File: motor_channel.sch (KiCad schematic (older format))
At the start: 1 part

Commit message: added jtag programming header for uC
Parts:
- U?: symbol hbridge:PWD13F60 -> bangbang_rev1-rescue:PWD13F60-hbridge
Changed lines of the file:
@@
 EESchema Schematic File Version 4
-LIBS:bangbang_rev1-cache
 EELAYER 30 0
 EELAYER END
@@
 $EndDescr
 $Comp
-L hbridge:PWD13F60 U?
+L bangbang_rev1-rescue:PWD13F60-hbridge U?
 U 1 1 5E507B4D
 P 3450 2900
+AR Path="/5E507B4D" Ref="U?"  Part="1"
+AR Path="/5E49EA18/5E507A5C/5E507B4D" Ref="U?"  Part="1"
 F 0 "U?" H 3450 3667 50  0000 C CNN
 F 1 "PWD13F60" H 3450 3576 50  0000 C CNN

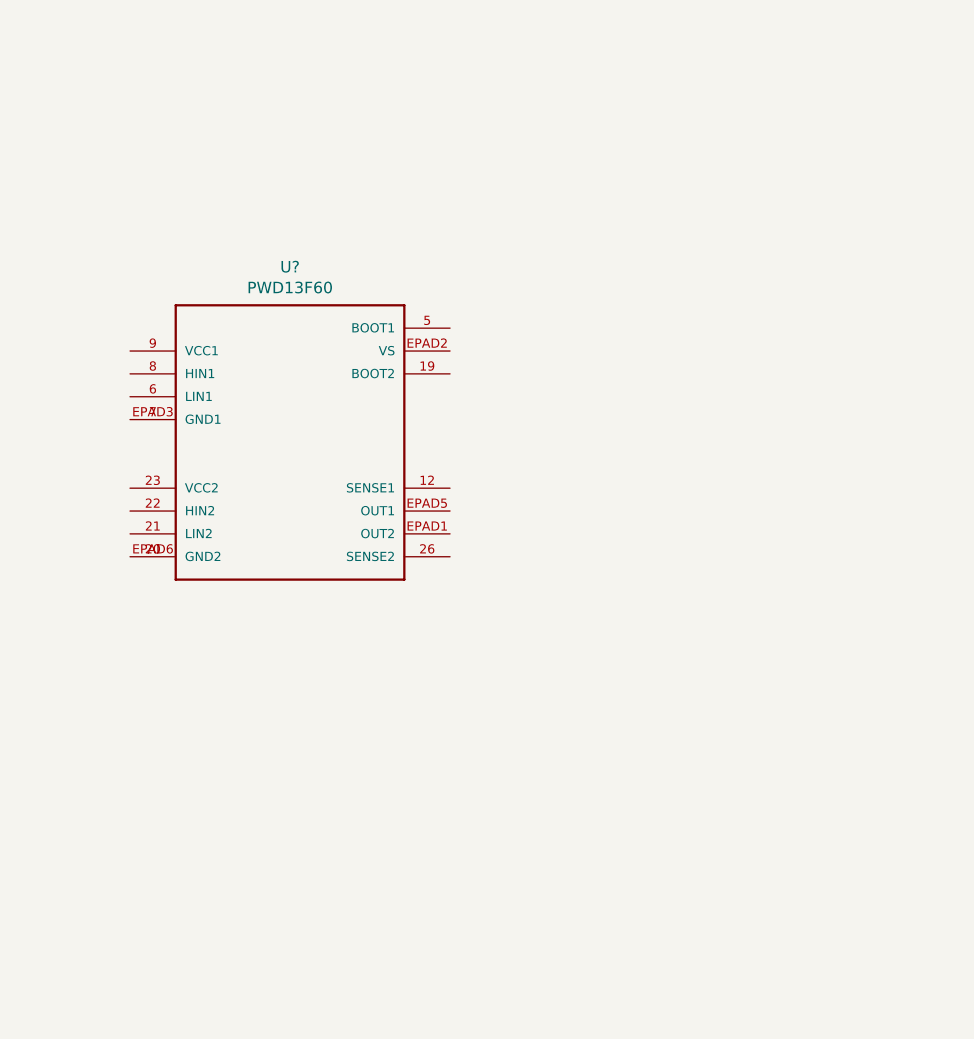
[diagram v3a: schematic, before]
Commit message: Motor channels mostly finished
Todo: Need to determine capacitance of decoupling caps in motor channel.
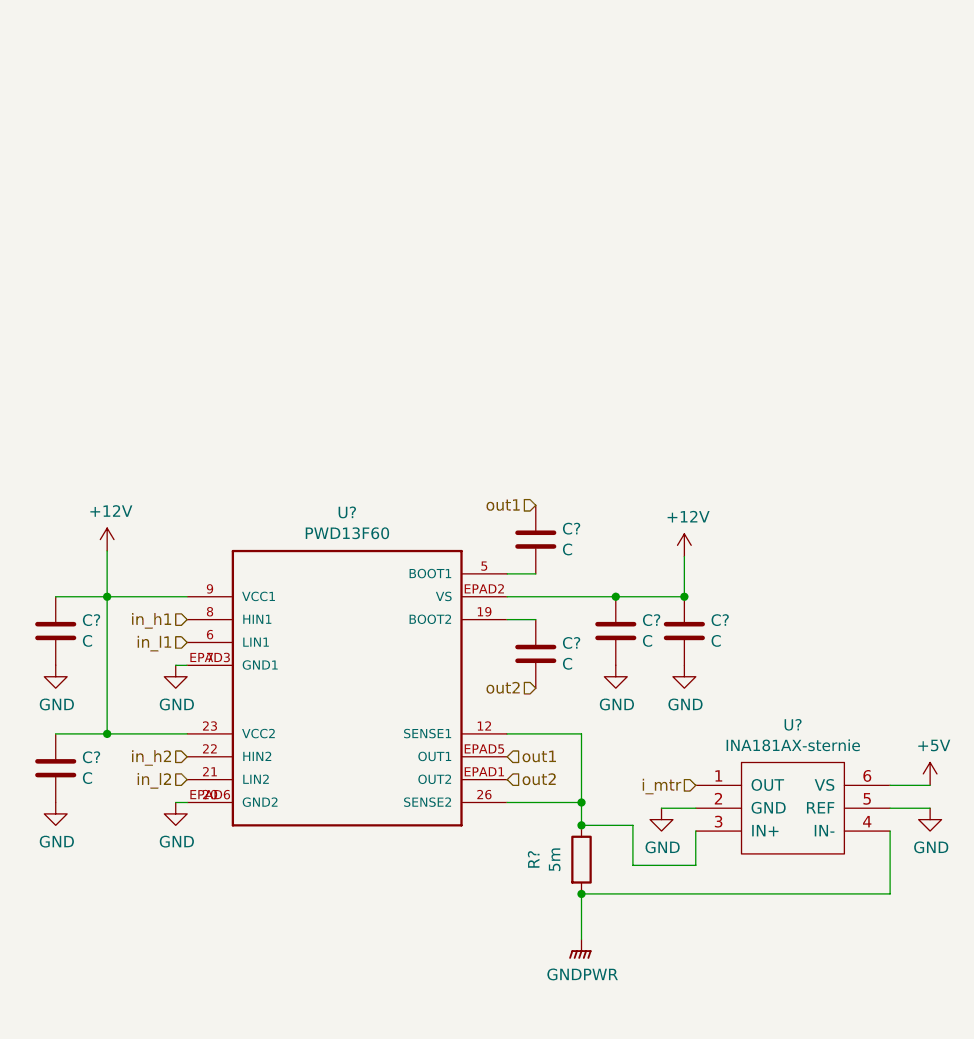
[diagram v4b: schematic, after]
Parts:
- added C? (x6): C, symbol Device:C
- added R?: 5m, symbol Device:R
- added U?: INA181AX-sternie, symbol bangbang_rev1-rescue:INA181AX-sternie
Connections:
- net at U?.12 (SENSE1): now also U?.26 (SENSE2), R?.1, U?.3 (IN+)
- net at U?.19 (BOOT2): now also C?.1
- net GND: now reaches U?.20 (GND2), U?.EPAD6 (GND2)
- net GND: now also U?.7 (GND1), U?.EPAD3 (GND1), C?.2, C?.2, C?.2, C?.2, U?.2 (GND), U?.5 (REF)
- net in_l2: now reaches U?.21 (LIN2)
- net in_h2: now reaches U?.22 (HIN2)
- net +12V: now reaches U?.23 (VCC2)
- net +12V: now also U?.9 (VCC1), U?.EPAD2 (VS), C?.1, C?.1, C?.1, C?.1
- net at U?.5 (BOOT1): now also C?.2
- net in_l1: now reaches U?.6 (LIN1)
- net in_h1: now reaches U?.8 (HIN1)
- net out2: now reaches U?.EPAD1 (OUT2)
- net out2: now also C?.2
- net out1: now reaches U?.EPAD5 (OUT1)
- net out1: now also C?.1
- new net +5V: U?.6 (VS)
- new net GNDPWR: R?.2, U?.4 (IN-)
- new net i_mtr: U?.1 (OUT)
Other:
- moved on the sheet: U?

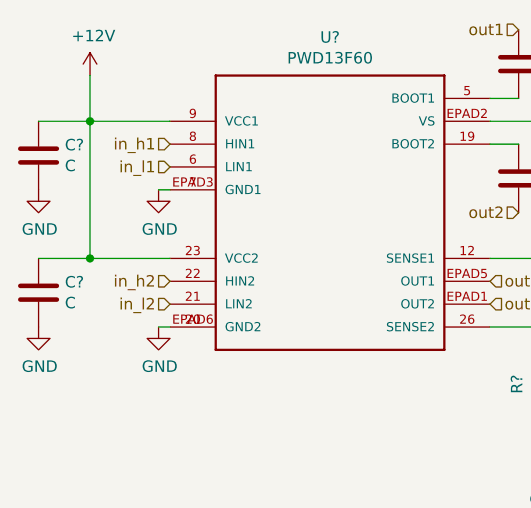
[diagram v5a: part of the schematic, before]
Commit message: Updated Motor Channels
Each motor only needs two inputs.
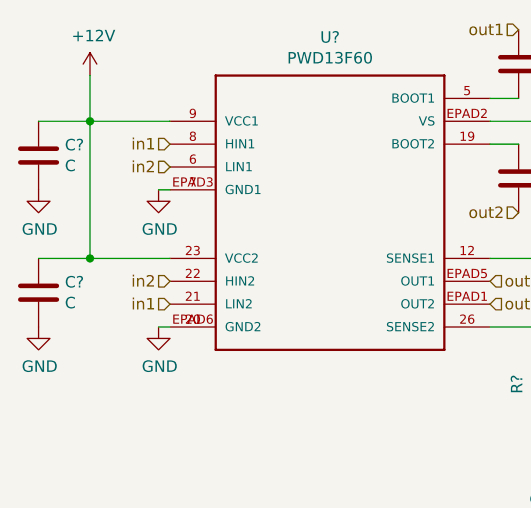
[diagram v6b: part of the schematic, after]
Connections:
- net in_l1 is gone; now on net in2: U?.6 (LIN1)
- net in_l2 is gone; now on net in1: U?.21 (LIN2)
- net in_h1 renamed in1
- net in_h2 renamed in2
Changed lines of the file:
@@
 AR Path="/5E49EA18/5E507A5C/5E507B4D" Ref="U?"  Part="1"
 AR Path="/5E49EA18/5E6AD26A/5E507B4D" Ref="U?"  Part="1"
+AR Path="/5E49EA18/5E6EF1BC/5E507B4D" Ref="U?"  Part="1"
 F 0 "U?" H 3700 4742 50  0000 C CNN
 F 1 "PWD13F60" H 3700 4651 50  0000 C CNN
@@
 AR Path="/5E49EA18/5E507A5C/5E6371F6" Ref="R?"  Part="1"
 AR Path="/5E49EA18/5E6AD26A/5E6371F6" Ref="R?"  Part="1"
+AR Path="/5E49EA18/5E6EF1BC/5E6371F6" Ref="R?"  Part="1"
 F 0 "R?" V 4518 4725 50  0000 C CNN
 F 1 "5m" V 4609 4725 50  0000 C CNN
@@
 AR Path="/5E49EA18/5E507A5C/5E634929" Ref="U?"  Part="1"
 AR Path="/5E49EA18/5E6AD26A/5E634929" Ref="U?"  Part="1"
+AR Path="/5E49EA18/5E6EF1BC/5E634929" Ref="U?"  Part="1"
 F 0 "U?" H 5650 4863 49  0000 C CNN
 F 1 "INA181AX-sternie" H 5650 4773 49  0000 C CNN
@@
 AR Path="/5E49EA18/5E507A5C/5E660BF5" Ref="#PWR?"  Part="1"
 AR Path="/5E49EA18/5E6AD26A/5E660BF5" Ref="#PWR?"  Part="1"
+AR Path="/5E49EA18/5E6EF1BC/5E660BF5" Ref="#PWR?"  Part="1"
 F 0 "#PWR?" H 6250 4250 50  0001 C CNN
 F 1 "GND" H 6255 4327 50  0000 C CNN
@@
 AR Path="/5E49EA18/5E507A5C/5E66287A" Ref="#PWR?"  Part="1"
 AR Path="/5E49EA18/5E6AD26A/5E66287A" Ref="#PWR?"  Part="1"
+AR Path="/5E49EA18/5E6EF1BC/5E66287A" Ref="#PWR?"  Part="1"
 F 0 "#PWR?" H 6250 4250 50  0001 C CNN
 F 1 "+5V" H 6265 4573 50  0000 C CNN
@@
 AR Path="/5E49EA18/5E507A5C/5E663717" Ref="#PWR?"  Part="1"
 AR Path="/5E49EA18/5E6AD26A/5E663717" Ref="#PWR?"  Part="1"
+AR Path="/5E49EA18/5E6EF1BC/5E663717" Ref="#PWR?"  Part="1"
 F 0 "#PWR?" H 5075 4250 50  0001 C CNN
 F 1 "GND" H 5080 4327 50  0000 C CNN
@@
 AR Path="/5E49EA18/5E507A5C/5E685700" Ref="#PWR?"  Part="1"
 AR Path="/5E49EA18/5E6AD26A/5E685700" Ref="#PWR?"  Part="1"
+AR Path="/5E49EA18/5E6EF1BC/5E685700" Ref="#PWR?"  Part="1"
 F 0 "#PWR?" H 2650 3225 50  0001 C CNN
 F 1 "+12V" H 2665 3548 50  0000 C CNN
@@
 	4725 4475 4400 4475
 Text HLabel 3000 3675 0    50   Input ~ 0
-in_h1
+in1
 Text HLabel 3000 3775 0    50   Input ~ 0
-in_l1
+in2
 Text HLabel 3000 4275 0    50   Input ~ 0
-in_h2
+in2
 Text HLabel 3000 4375 0    50   Input ~ 0
-in_l2
+in1
 Wire Wire Line
 	2650 4175 2650 3575
@@
 U 1 1 5E6C0524
 P 4725 5075
+AR Path="/5E49EA18/5E507A5C/5E6C0524" Ref="#PWR?"  Part="1"
+AR Path="/5E49EA18/5E6EF1BC/5E6C0524" Ref="#PWR?"  Part="1"
 F 0 "#PWR?" H 4725 4875 50  0001 C CNN
 F 1 "GNDPWR" H 4729 4921 50  0000 C CNN
@@
 U 1 1 5E6C2BF6
 P 2950 3875
+AR Path="/5E49EA18/5E507A5C/5E6C2BF6" Ref="#PWR?"  Part="1"
+AR Path="/5E49EA18/5E6EF1BC/5E6C2BF6" Ref="#PWR?"  Part="1"
 F 0 "#PWR?" H 2950 3625 50  0001 C CNN
 F 1 "GND" H 2955 3702 50  0000 C CNN
@@
 U 1 1 5E6C314D
 P 2950 4475
+AR Path="/5E49EA18/5E507A5C/5E6C314D" Ref="#PWR?"  Part="1"
+AR Path="/5E49EA18/5E6EF1BC/5E6C314D" Ref="#PWR?"  Part="1"
 F 0 "#PWR?" H 2950 4225 50  0001 C CNN
 F 1 "GND" H 2955 4302 50  0000 C CNN
@@
 U 1 1 5E6C3B2F
 P 2425 3725
+AR Path="/5E49EA18/5E507A5C/5E6C3B2F" Ref="C?"  Part="1"
+AR Path="/5E49EA18/5E6EF1BC/5E6C3B2F" Ref="C?"  Part="1"
 F 0 "C?" H 2540 3771 50  0000 L CNN
 F 1 "C" H 2540 3680 50  0000 L CNN
@@
 U 1 1 5E6C48A1
 P 2425 4325
+AR Path="/5E49EA18/5E507A5C/5E6C48A1" Ref="C?"  Part="1"
+AR Path="/5E49EA18/5E6EF1BC/5E6C48A1" Ref="C?"  Part="1"
 F 0 "C?" H 2540 4371 50  0000 L CNN
 F 1 "C" H 2540 4280 50  0000 L CNN
@@
 U 1 1 5E6C5CF4
 P 2425 3875
+AR Path="/5E49EA18/5E507A5C/5E6C5CF4" Ref="#PWR?"  Part="1"
+AR Path="/5E49EA18/5E6EF1BC/5E6C5CF4" Ref="#PWR?"  Part="1"
 F 0 "#PWR?" H 2425 3625 50  0001 C CNN
 F 1 "GND" H 2430 3702 50  0000 C CNN
@@
 U 1 1 5E6C6240
 P 2425 4475
+AR Path="/5E49EA18/5E507A5C/5E6C6240" Ref="#PWR?"  Part="1"
+AR Path="/5E49EA18/5E6EF1BC/5E6C6240" Ref="#PWR?"  Part="1"
 F 0 "#PWR?" H 2425 4225 50  0001 C CNN
 F 1 "GND" H 2430 4302 50  0000 C CNN
@@
 U 1 1 5E6C6CA0
 P 4525 3325
+AR Path="/5E49EA18/5E507A5C/5E6C6CA0" Ref="C?"  Part="1"
+AR Path="/5E49EA18/5E6EF1BC/5E6C6CA0" Ref="C?"  Part="1"
 F 0 "C?" H 4640 3371 50  0000 L CNN
 F 1 "C" H 4640 3280 50  0000 L CNN
@@
 U 1 1 5E6C896D
 P 4525 3825
+AR Path="/5E49EA18/5E507A5C/5E6C896D" Ref="C?"  Part="1"
+AR Path="/5E49EA18/5E6EF1BC/5E6C896D" Ref="C?"  Part="1"
 F 0 "C?" H 4640 3871 50  0000 L CNN
 F 1 "C" H 4640 3780 50  0000 L CNN
@@
 U 1 1 5E6CC77E
 P 5175 3400
+AR Path="/5E49EA18/5E507A5C/5E6CC77E" Ref="#PWR?"  Part="1"
+AR Path="/5E49EA18/5E6EF1BC/5E6CC77E" Ref="#PWR?"  Part="1"
 F 0 "#PWR?" H 5175 3250 50  0001 C CNN
 F 1 "+12V" H 5190 3573 50  0000 C CNN
@@
 U 1 1 5E6CD1E7
 P 4875 3725
+AR Path="/5E49EA18/5E507A5C/5E6CD1E7" Ref="C?"  Part="1"
+AR Path="/5E49EA18/5E6EF1BC/5E6CD1E7" Ref="C?"  Part="1"
 F 0 "C?" H 4990 3771 50  0000 L CNN
 F 1 "C" H 4990 3680 50  0000 L CNN
@@
 U 1 1 5E6CE986
 P 5175 3725
+AR Path="/5E49EA18/5E507A5C/5E6CE986" Ref="C?"  Part="1"
+AR Path="/5E49EA18/5E6EF1BC/5E6CE986" Ref="C?"  Part="1"
 F 0 "C?" H 5290 3771 50  0000 L CNN
 F 1 "C" H 5290 3680 50  0000 L CNN
@@
 U 1 1 5E6D07E0
 P 4875 3875
+AR Path="/5E49EA18/5E507A5C/5E6D07E0" Ref="#PWR?"  Part="1"
+AR Path="/5E49EA18/5E6EF1BC/5E6D07E0" Ref="#PWR?"  Part="1"
 F 0 "#PWR?" H 4875 3625 50  0001 C CNN
 F 1 "GND" H 4880 3702 50  0000 C CNN
@@
 U 1 1 5E6D0C7C
 P 5175 3875
+AR Path="/5E49EA18/5E507A5C/5E6D0C7C" Ref="#PWR?"  Part="1"
+AR Path="/5E49EA18/5E6EF1BC/5E6D0C7C" Ref="#PWR?"  Part="1"
 F 0 "#PWR?" H 5175 3625 50  0001 C CNN
 F 1 "GND" H 5180 3702 50  0000 C CNN

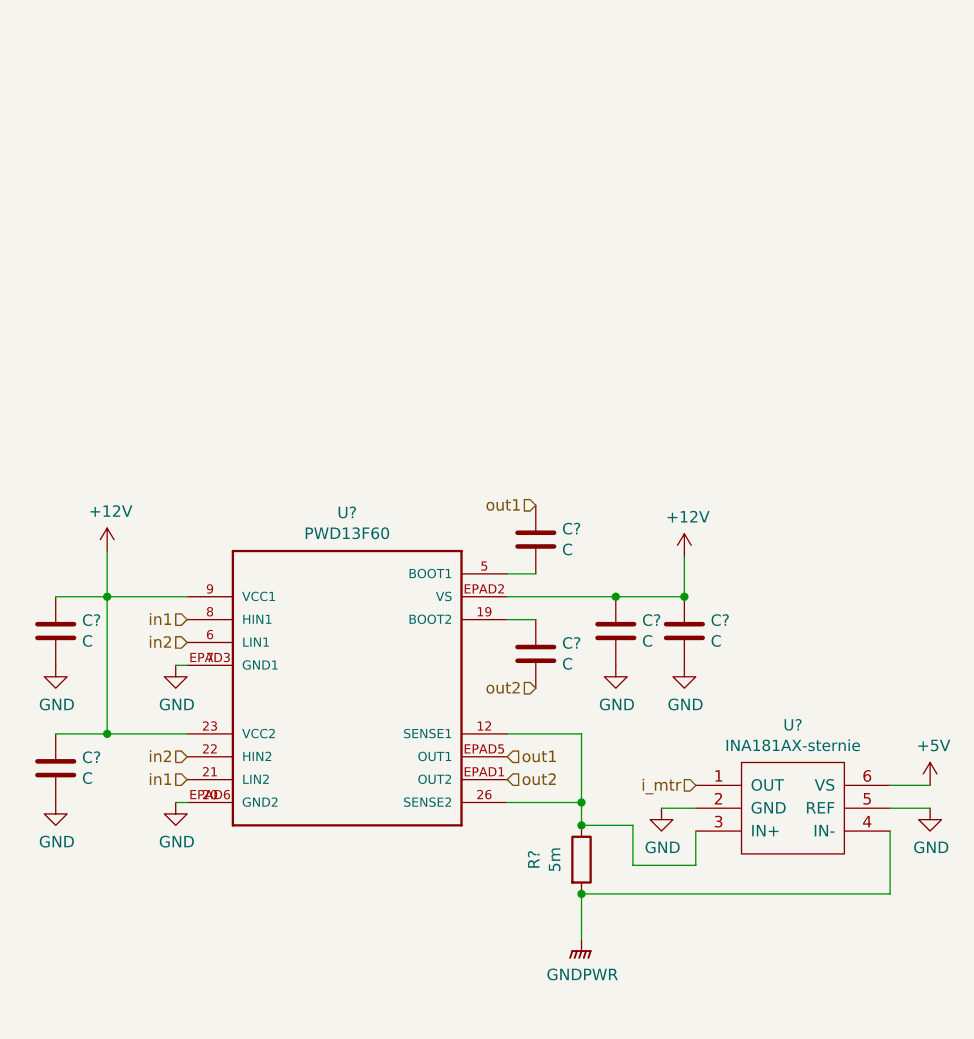
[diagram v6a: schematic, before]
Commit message: added dual inpt and gate control
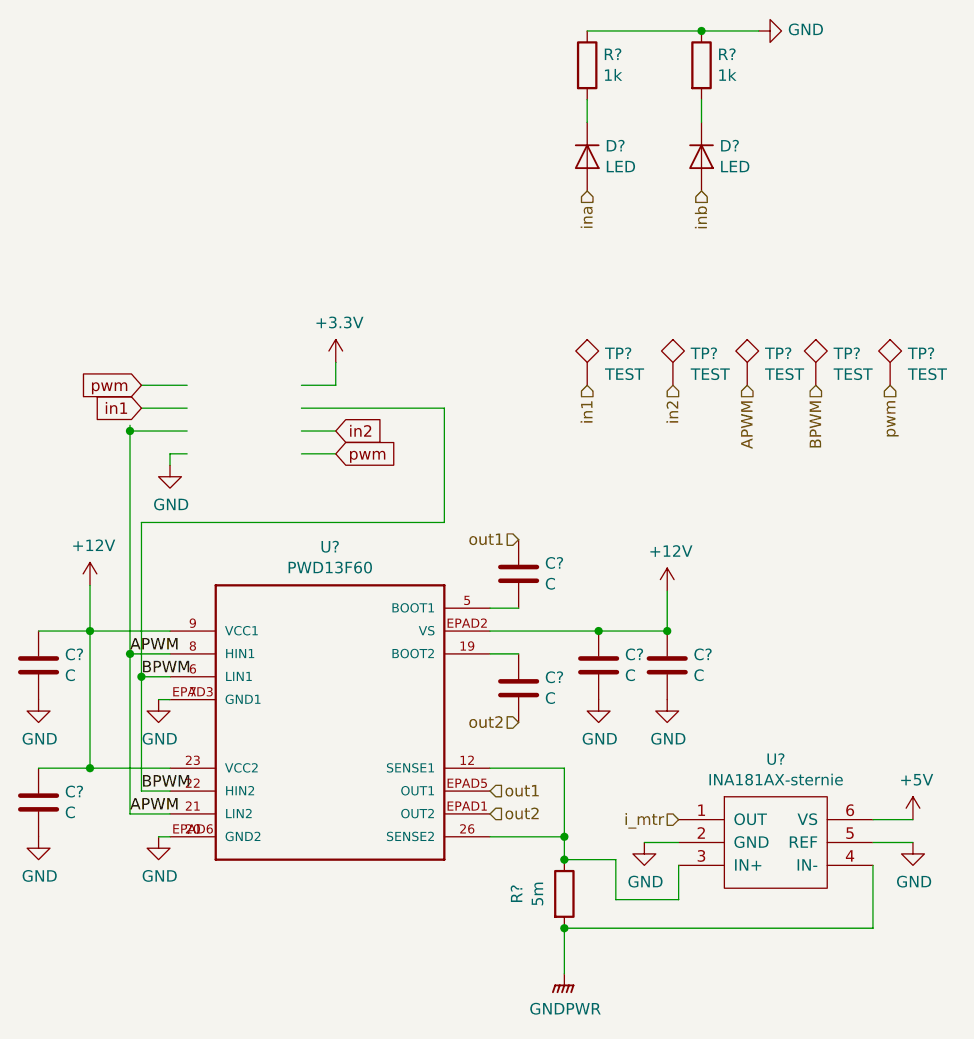
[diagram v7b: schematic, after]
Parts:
- added D? (x2): LED, symbol Device:D
- added R? (x2): 1k, symbol Device:R
- added TP? (x5): TEST, symbol Engine_Controller-cache:TEST
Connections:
- net labels added: +3.3V, APWM, BPWM, ina, inb, pwm
- wire segments 27 -> 52
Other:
- moved on the sheet: C?, R?, U?

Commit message: Added AND gate footprint
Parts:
- added U?: 74AHC2G08, symbol ec_2b_rescue:74AHC2G08
- TP? (x5): symbol Engine_Controller-cache:TEST -> bangbang_rev1-rescue:TEST-Engine_Controller-cache
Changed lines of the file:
@@
 $Descr A4 11693 8268
 encoding utf-8
-Sheet 12 12
+Sheet 11 12
 Title ""
 Date ""
@@
 in1
 Wire Wire Line
-	3500 2650 3650 2650
-Wire Wire Line
-	3650 2650 3650 2550
-Wire Wire Line
-	3500 2850 3650 2850
-Wire Wire Line
-	3500 2950 3650 2950
-Text GLabel 3650 2850 2    50   Input ~ 0
+	3900 2650 4050 2650
+Wire Wire Line
+	4050 2650 4050 2550
+Wire Wire Line
+	3900 2850 4050 2850
+Wire Wire Line
+	3900 2950 4050 2950
+Text GLabel 4050 2850 2    50   Input ~ 0
 in2
-Text GLabel 3650 2950 2    50   Input ~ 0
+Text GLabel 4050 2950 2    50   Input ~ 0
 pwm
 Wire Wire Line
@@
 	2750 3825 2750 4525
 Wire Wire Line
-	4125 2750 4125 3250
-Wire Wire Line
-	4125 3250 2800 3250
-Wire Wire Line
 	2800 3250 2800 3925
 Wire Wire Line
 	2800 4425 2925 4425
-Wire Wire Line
-	3500 2750 4125 2750
 Wire Wire Line
 	2925 3925 2800 3925
@@
 L power:+3.3V #PWR?
 U 1 1 5E666730
-P 3650 2550
+P 4050 2550
 AR Path="/5E49EA18/5E507A5C/5E666730" Ref="#PWR?"  Part="1"
 AR Path="/5E49EA18/5E6EF1BC/5E666730" Ref="#PWR?"  Part="1"
-F 0 "#PWR?" H 3650 2400 50  0001 C CNN
-F 1 "+3.3V" H 3665 2723 50  0000 C CNN
-F 2 "" H 3650 2550 50  0001 C CNN
-F 3 "" H 3650 2550 50  0001 C CNN
-	1    3650 2550
+F 0 "#PWR?" H 4050 2400 50  0001 C CNN
+F 1 "+3.3V" H 4065 2723 50  0000 C CNN
+F 2 "" H 4050 2550 50  0001 C CNN
+F 3 "" H 4050 2550 50  0001 C CNN
+	1    4050 2550
 	1    0    0    -1
 $EndComp
@@
 	2925 2950 3000 2950
 $Comp
-L Engine_Controller-cache:GND #PWR?
+L bangbang_rev1-rescue:GND-Engine_Controller-cache #PWR?
 U 1 1 5E669D2E
 P 2925 3000
 AR Path="/5E49EA18/5E507A5C/5E669D2E" Ref="#PWR?"  Part="1"
 AR Path="/5E49EA18/5E6EF1BC/5E669D2E" Ref="#PWR?"  Part="1"
+AR Path="/5E669D2E" Ref="#PWR?"  Part="1"
 F 0 "#PWR?" H 2925 2750 50  0001 C CNN
 F 1 "GND" H 2930 2827 50  0000 C CNN
@@
 $EndComp
 $Comp
-L Engine_Controller-cache:TEST TP?
+L bangbang_rev1-rescue:TEST-Engine_Controller-cache TP?
 U 1 1 5E66AC4A
 P 4750 2650
@@
 $EndComp
 $Comp
-L Engine_Controller-cache:TEST TP?
+L bangbang_rev1-rescue:TEST-Engine_Controller-cache TP?
 U 1 1 5E66B0FC
 P 5125 2650
@@
 $EndComp
 $Comp
-L Engine_Controller-cache:TEST TP?
+L bangbang_rev1-rescue:TEST-Engine_Controller-cache TP?
 U 1 1 5E66BCEE
 P 5450 2650
@@
 $EndComp
 $Comp
-L Engine_Controller-cache:TEST TP?
+L bangbang_rev1-rescue:TEST-Engine_Controller-cache TP?
 U 1 1 5E66CBC1
 P 5750 2650
@@
 $EndComp
 $Comp
-L Engine_Controller-cache:TEST TP?
+L bangbang_rev1-rescue:TEST-Engine_Controller-cache TP?
 U 1 1 5E66CBC7
 P 6075 2650
@@
 	5250 1100 5500 1100
 $Comp
-L Engine_Controller-cache:GND #PWR?
+L bangbang_rev1-rescue:GND-Engine_Controller-cache #PWR?
 U 1 1 5E676C32
 P 5500 1100
 AR Path="/5E49EA18/5E507A5C/5E676C32" Ref="#PWR?"  Part="1"
 AR Path="/5E49EA18/5E6EF1BC/5E676C32" Ref="#PWR?"  Part="1"
+AR Path="/5E676C32" Ref="#PWR?"  Part="1"
 F 0 "#PWR?" H 5500 850 50  0001 C CNN
 F 1 "GND" V 5505 972 50  0000 R CNN
@@
 	0    -1   -1   0
 $EndComp
+$Comp
+L ec_2b_rescue:74AHC2G08 U?
+U 1 1 5E659488
+P 3000 2350
+F 0 "U?" H 3450 2337 60  0000 C CNN
+F 1 "74AHC2G08" H 3450 2231 60  0000 C CNN
+F 2 "" H 3000 2350 60  0001 C CNN
+F 3 "" H 3000 2350 60  0001 C CNN
+	1    3000 2350
+	1    0    0    -1
+$EndComp
+Wire Wire Line
+	3900 2750 4300 2750
+Wire Wire Line
+	4300 2750 4300 3250
+Wire Wire Line
+	2800 3250 4300 3250
 $EndSCHEMATC
